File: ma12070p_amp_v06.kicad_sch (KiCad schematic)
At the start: 85 parts, among them U1 MAX16956AUBD/V+, U2 MA12070P

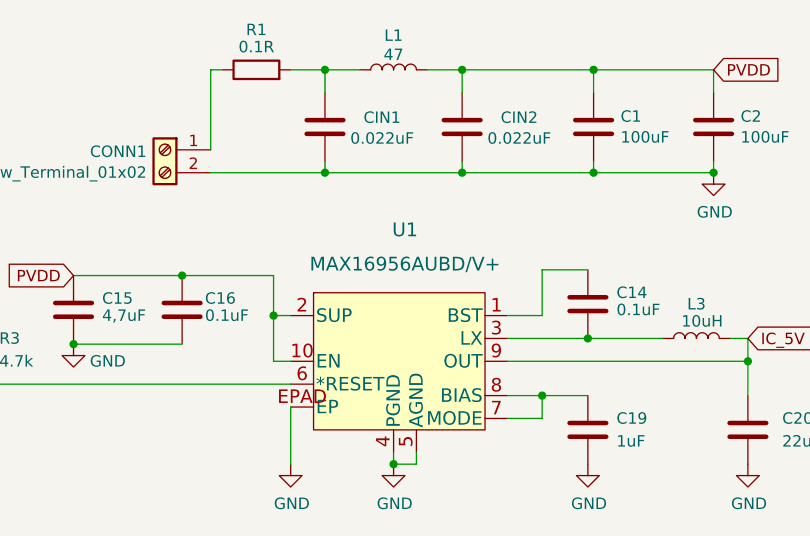
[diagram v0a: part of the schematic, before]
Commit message: updated dcdc  converter
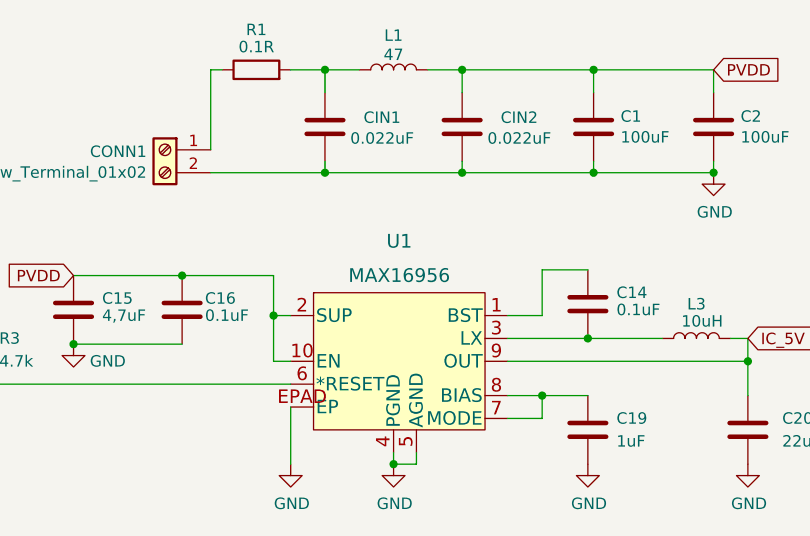
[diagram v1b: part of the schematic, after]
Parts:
- U1: value MAX16956AUBD/V+ -> MAX16956
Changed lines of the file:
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@@
   (symbol (lib_id "max_16956:MAX16956AUBD{slash}V+") (at 68.58 56.515 0) (unit 1)
     (in_bom yes) (on_board yes) (fields_autoplaced)
-    (property "Reference" "U1" (id 0) (at 68.58 41.91 0)
+    (property "Reference" "U1" (id 0) (at 67.945 43.18 0)
       (effects (font (size 1.524 1.524)))
     )
-    (property "Value" "MAX16956AUBD/V+" (id 1) (at 68.58 45.72 0)
+    (property "Value" "MAX16956" (id 1) (at 67.945 46.99 0)
       (effects (font (size 1.524 1.524)))
     )
@@
     )
     (path "/be568931-994d-4a64-b4e6-f6775e31820a"
-      (reference "U1") (unit 1) (value "MAX16956AUBD/V+") (footprint "max_16956:MAX16956AUBD&slash_V&plus_")
+      (reference "U1") (unit 1) (value "MAX16956") (footprint "max_16956:MAX16956AUBD&slash_V&plus_")
     )
     (path "/783e136e-630e-48ef-abfe-dc99a550ed24"

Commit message: created gerber
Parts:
- removed C32, C33: 10uF, Capacitor_SMD:C_1206_3216Metric_Pad1.33x1.80mm_HandSolder, symbol Device:C
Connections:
- net VDD is gone; now on net GND: C37.1, C42.1, C7.1, JP1.2 (C), JP10.3 (B), JP3.3 (B), JP4.1 (A), JP5.3 (B), JP9.3 (B), LED1.2 (A), LED2.2 (A), R3.1, U2.17 (AVDD), U2.55 (DVDD)
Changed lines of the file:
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@@
   (junction (at 243.205 121.92) (diameter 0) (color 0 0 0 0)
   )
-  (junction (at 106.045 90.805) (diameter 0) (color 0 0 0 0)
+  (junction (at 92.71 90.805) (diameter 0) (color 0 0 0 0)
   )
   (junction (at 59.69 24.13) (diameter 0) (color 0 0 0 0)
@@
   (junction (at 156.845 140.335) (diameter 0) (color 0 0 0 0)
   )
-  (junction (at 95.885 90.805) (diameter 0) (color 0 0 0 0)
-  )
   (junction (at 243.205 132.08) (diameter 0) (color 0 0 0 0)
   )
@@
     (stroke (width 0) (type default) (color 0 0 0 0))
   )
-  (wire (pts (xy 106.045 100.965) (xy 106.045 99.695))
-    (stroke (width 0) (type default) (color 0 0 0 0))
-  )
   (wire (pts (xy 178.435 120.015) (xy 178.435 122.555))
     (stroke (width 0) (type default) (color 0 0 0 0))
@@
     (stroke (width 0) (type default) (color 0 0 0 0))
   )
-  (wire (pts (xy 95.885 92.075) (xy 95.885 90.805))
-    (stroke (width 0) (type default) (color 0 0 0 0))
-  )
   (wire (pts (xy 80.01 60.325) (xy 83.82 60.325))
     (stroke (width 0) (type default) (color 0 0 0 0))
@@
     (stroke (width 0) (type default) (color 0 0 0 0))
   )
-  (wire (pts (xy 95.885 99.695) (xy 95.885 100.965))
-    (stroke (width 0) (type default) (color 0 0 0 0))
-  )
   (wire (pts (xy 41.275 130.81) (xy 41.275 132.715))
     (stroke (width 0) (type default) (color 0 0 0 0))
@@
     (stroke (width 0) (type default) (color 0 0 0 0))
   )
-  (wire (pts (xy 95.885 90.805) (xy 106.045 90.805))
-    (stroke (width 0) (type default) (color 0 0 0 0))
-  )
   (wire (pts (xy 83.82 62.865) (xy 83.82 60.325))
     (stroke (width 0) (type default) (color 0 0 0 0))
@@
     (stroke (width 0) (type default) (color 0 0 0 0))
   )
-  (wire (pts (xy 88.265 90.805) (xy 95.885 90.805))
+  (wire (pts (xy 88.265 90.805) (xy 92.71 90.805))
     (stroke (width 0) (type default) (color 0 0 0 0))
   )
@@
     (stroke (width 0) (type default) (color 0 0 0 0))
   )
-  (wire (pts (xy 106.045 90.805) (xy 106.045 92.075))
+  (wire (pts (xy 92.71 90.805) (xy 92.71 93.345))
     (stroke (width 0) (type default) (color 0 0 0 0))
   )
@@
     (pin "2")
   )
-  (symbol (lib_id "Device:C") (at 95.885 95.885 0) (mirror x) (unit 1)
+  (symbol (lib_id "power:GND") (at 92.71 93.345 0) (unit 1)
     (in_bom yes) (on_board yes)
-    (property "Reference" "C32" (id 0) (at 102.2858 95.885 90))
-    (property "Value" "10uF" (id 1) (at 99.9744 95.885 90))
-    (property "Footprint" "Capacitor_SMD:C_1206_3216Metric_Pad1.33x1.80mm_HandSolder" (id 2) (at 96.8502 92.075 0)
+    (property "Reference" "#PWR019" (id 0) (at 92.71 99.695 0)
       (effects (font (size 1.27 1.27)) hide)
     )
-    (property "Datasheet" "~" (id 3) (at 95.885 95.885 0)
+    (property "Value" "GND" (id 1) (at 92.837 97.7392 0))
+    (property "Footprint" "" (id 2) (at 92.71 93.345 0)
       (effects (font (size 1.27 1.27)) hide)
     )
-    (property "infineonRef" "COUNTBUCK0" (id 4) (at 95.885 95.885 0)
-      (effects (font (size 1.27 1.27)) hide)
-    )
-    (property "property_2" "50V" (id 5) (at 95.885 95.885 0)
-      (effects (font (size 1.27 1.27)) hide)
-    )
-    (pin "1")
-    (pin "2")
-  )
-  (symbol (lib_id "power:GND") (at 95.885 100.965 0) (unit 1)
-    (in_bom yes) (on_board yes)
-    (property "Reference" "#PWR018" (id 0) (at 95.885 107.315 0)
-      (effects (font (size 1.27 1.27)) hide)
-    )
-    (property "Value" "GND" (id 1) (at 96.012 105.3592 0))
-    (property "Footprint" "" (id 2) (at 95.885 100.965 0)
-      (effects (font (size 1.27 1.27)) hide)
-    )
-    (property "Datasheet" "" (id 3) (at 95.885 100.965 0)
-      (effects (font (size 1.27 1.27)) hide)
-    )
-    (pin "1")
-  )
-  (symbol (lib_id "Device:C") (at 106.045 95.885 0) (mirror x) (unit 1)
-    (in_bom yes) (on_board yes)
-    (property "Reference" "C33" (id 0) (at 112.4458 95.885 90))
-    (property "Value" "10uF" (id 1) (at 110.1344 95.885 90))
-    (property "Footprint" "Capacitor_SMD:C_1206_3216Metric_Pad1.33x1.80mm_HandSolder" (id 2) (at 107.0102 92.075 0)
-      (effects (font (size 1.27 1.27)) hide)
-    )
-    (property "Datasheet" "~" (id 3) (at 106.045 95.885 0)
-      (effects (font (size 1.27 1.27)) hide)
-    )
-    (property "infineonRef" "COUNTBUCK1" (id 4) (at 106.045 95.885 0)
-      (effects (font (size 1.27 1.27)) hide)
-    )
-    (property "property_2" "50V" (id 5) (at 106.045 95.885 0)
-      (effects (font (size 1.27 1.27)) hide)
-    )
-    (pin "1")
-    (pin "2")
-  )
-  (symbol (lib_id "power:GND") (at 106.045 100.965 0) (unit 1)
-    (in_bom yes) (on_board yes)
-    (property "Reference" "#PWR019" (id 0) (at 106.045 107.315 0)
-      (effects (font (size 1.27 1.27)) hide)
-    )
-    (property "Value" "GND" (id 1) (at 106.172 105.3592 0))
-    (property "Footprint" "" (id 2) (at 106.045 100.965 0)
-      (effects (font (size 1.27 1.27)) hide)
-    )
-    (property "Datasheet" "" (id 3) (at 106.045 100.965 0)
+    (property "Datasheet" "" (id 3) (at 92.71 93.345 0)
       (effects (font (size 1.27 1.27)) hide)
     )
@@
     (pin "1")
   )
-  (symbol (lib_id "power:VDD") (at 106.045 90.805 0) (unit 1)
+  (symbol (lib_id "power:VDD") (at 92.71 90.805 0) (unit 1)
     (in_bom yes) (on_board yes)
-    (property "Reference" "#PWR014" (id 0) (at 106.045 94.615 0)
+    (property "Reference" "#PWR014" (id 0) (at 92.71 94.615 0)
       (effects (font (size 1.27 1.27)) hide)
     )
-    (property "Value" "VDD" (id 1) (at 106.045 86.995 0))
-    (property "Footprint" "" (id 2) (at 106.045 90.805 0)
+    (property "Value" "VDD" (id 1) (at 92.71 86.995 0))
+    (property "Footprint" "" (id 2) (at 92.71 90.805 0)
       (effects (font (size 1.27 1.27)) hide)
     )
-    (property "Datasheet" "" (id 3) (at 106.045 90.805 0)
+    (property "Datasheet" "" (id 3) (at 92.71 90.805 0)
       (effects (font (size 1.27 1.27)) hide)
     )
@@
       (reference "#PWR017") (unit 1) (value "VDD") (footprint "")
     )
-    (path "/00000000-0000-0000-0000-000060685e08"
-      (reference "#PWR018") (unit 1) (value "GND") (footprint "")
-    )
     (path "/00000000-0000-0000-0000-0000606a8e11"
       (reference "#PWR019") (unit 1) (value "GND") (footprint "")
@@
       (reference "C31") (unit 1) (value "0.1uF") (footprint "Capacitor_SMD:C_1206_3216Metric_Pad1.33x1.80mm_HandSolder")
     )
-    (path "/00000000-0000-0000-0000-000060652f5d"
-      (reference "C32") (unit 1) (value "10uF") (footprint "Capacitor_SMD:C_1206_3216Metric_Pad1.33x1.80mm_HandSolder")
-    )
-    (path "/00000000-0000-0000-0000-0000606a8893"
-      (reference "C33") (unit 1) (value "10uF") (footprint "Capacitor_SMD:C_1206_3216Metric_Pad1.33x1.80mm_HandSolder")
-    )
     (path "/00000000-0000-0000-0000-0000603142ea"

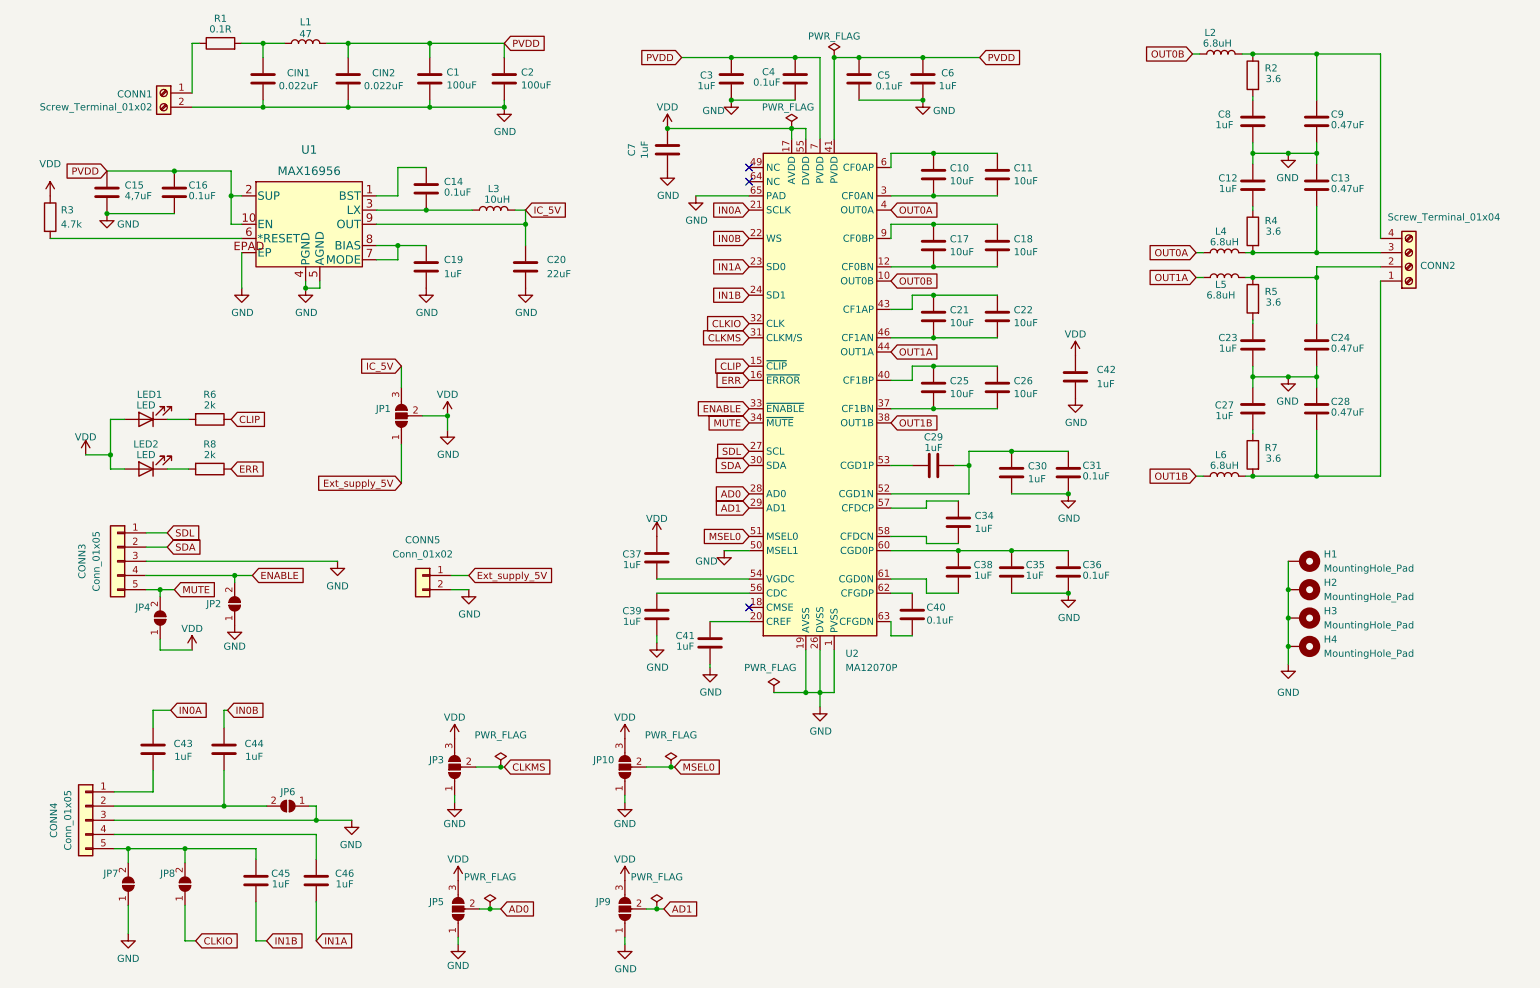
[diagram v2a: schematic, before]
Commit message: Fixed VDD traces
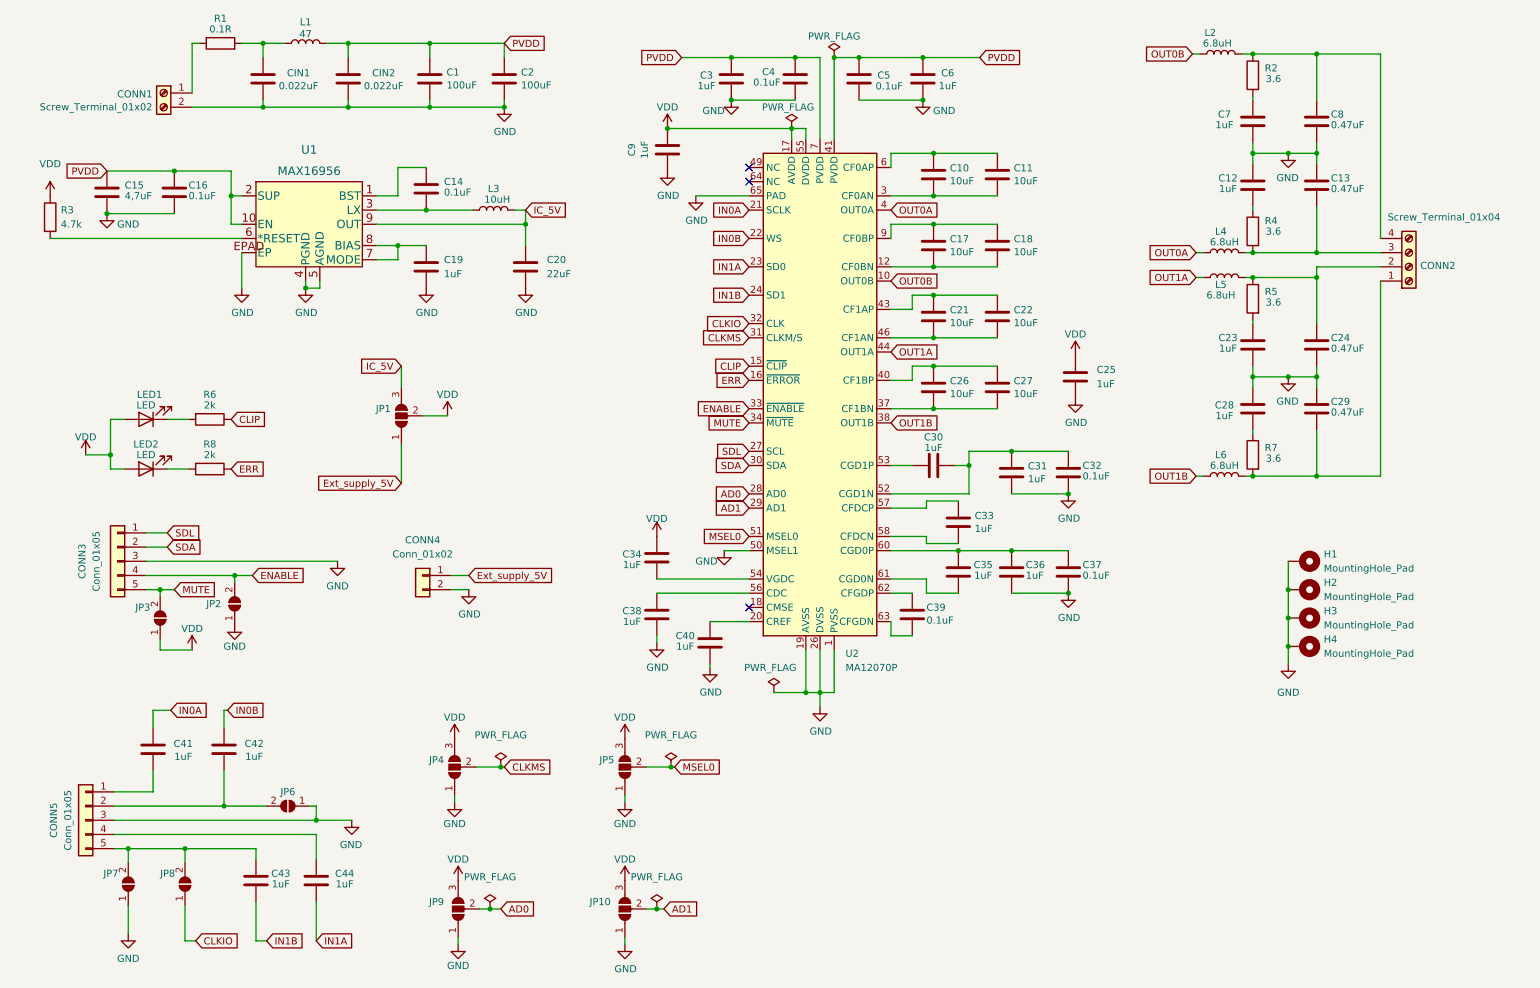
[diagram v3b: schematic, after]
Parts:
- renumbered C42 to C25, C25 to C26, C26 to C27, C27 to C28, C28 to C29, C29 to C30, C30 to C31, C31 to C32, C34 to C33, C37 to C34, C38 to C35, C35 to C36, C36 to C37, C39 to C38, C40 to C39, C41 to C40, C43 to C41, C44 to C42, C45 to C43, C46 to C44, C8 to C7, C9 to C8, C7 to C9, CONN5 to CONN4, CONN4 to CONN5, JP9 to JP10, JP4 to JP3, JP3 to JP4, JP10 to JP5, JP5 to JP9
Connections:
- net GND: no longer C25.1, C34.1, C9.1, JP1.2 (C), JP10.3 (B), JP3.1 (A), JP4.3 (B), JP5.3 (B), JP9.3 (B), LED1.2 (A), LED2.2 (A), R3.1, U2.17 (AVDD), U2.55 (DVDD)
- new net VDD: C25.1, C34.1, C9.1, JP1.2 (C), JP10.3 (B), JP3.1 (A), JP4.3 (B), JP5.3 (B), JP9.3 (B), LED1.2 (A), LED2.2 (A), R3.1, U2.17 (AVDD), U2.55 (DVDD)
